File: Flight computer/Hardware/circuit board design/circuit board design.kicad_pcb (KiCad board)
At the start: 4 copper layers, 31.7 x 82.6 mm, 86 parts, among them J1 Conn_01x04, J2 USB_B_Micro, J3 Screw_Terminal_01x04, J4 Conn_01x02, J5 Screw_Terminal_01x04, J6 Conn_Coaxial, J7 Conn_Coaxial, U1 IIS2MDC, U10 BMI088, U11 ATSAML21J18B-AUT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

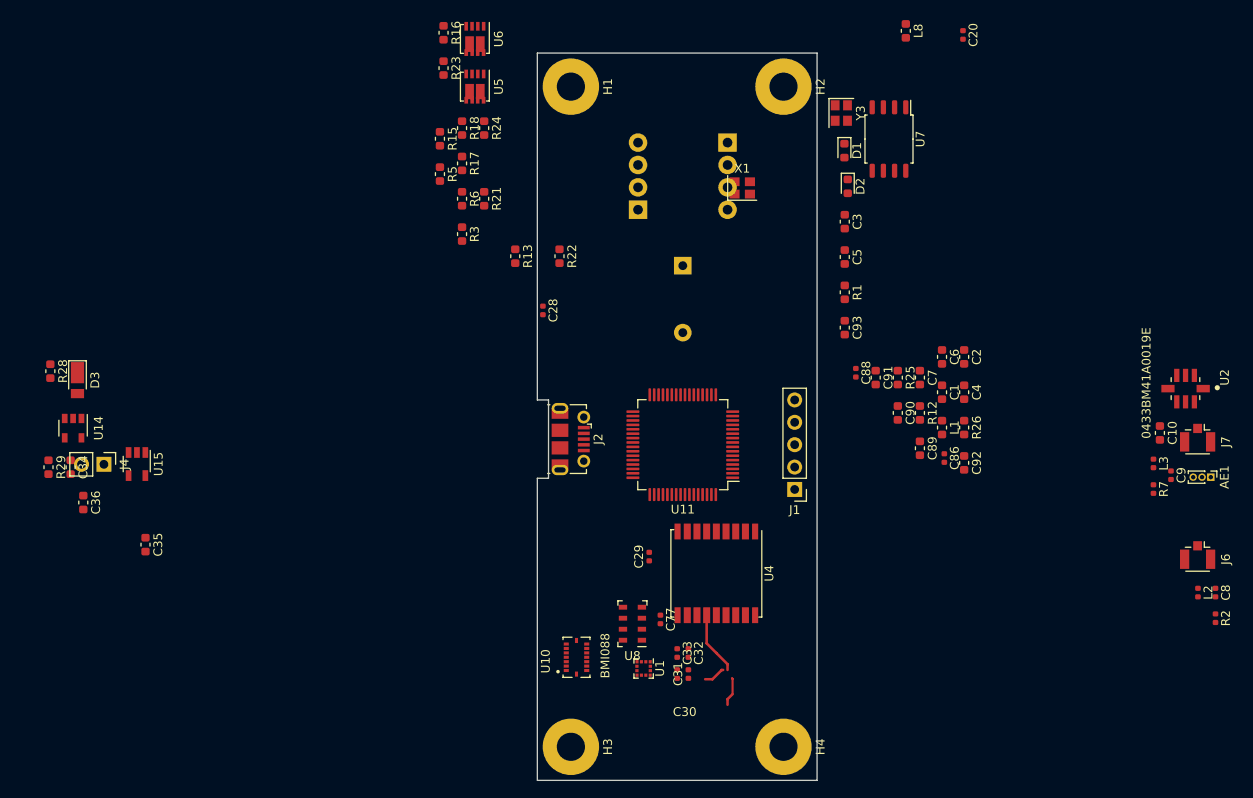
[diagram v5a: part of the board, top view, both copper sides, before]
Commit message: updated the datasheet links and sites to purchase
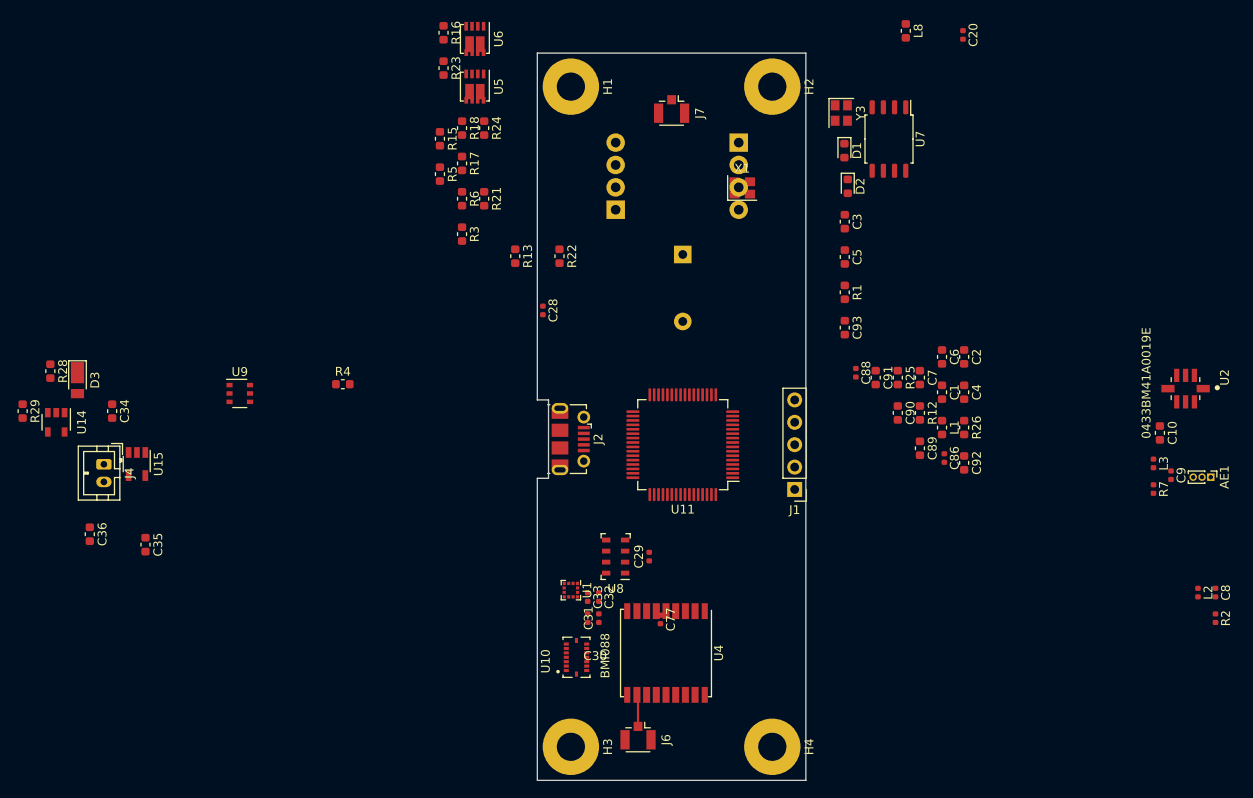
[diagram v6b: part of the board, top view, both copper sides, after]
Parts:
- added R4: 1K, Resistor_SMD:R_0603_1608Metric, F.Cu at (229.4, 284.0)
- added U9: STF202-22T1G, Package_SO:TSOP-6_1.65x3.05mm_P0.95mm, F.Cu at (217.7, 285.0)
- D1: value LED -> RED_LED
- D2: value LED -> BLUE_LED
- J1: value Conn_01x04 -> Conn_01x05
- J4: footprint Connector_PinHeader_2.54mm:PinHeader_1x02_P2.54mm_Vertical -> Connector_JST:JST_PH_B2B-PH-K_1x02_P2.00mm_Vertical
- moved J7 70.4 mm to (266.7, 252.7)
- moved J6 66.7 mm to (262.9, 323.9)
- moved U1 12.1 mm to (255.3, 307.3)
- moved C31 12.0 mm to (258.4, 310.5)
- moved C32 12.0 mm to (258.4, 308.1)
- moved C30 12.0 mm to (257.2, 310.5)
- moved C33 12.0 mm to (257.2, 308.1)
- moved U4 10.7 mm to (266.1, 314.5)
- moved C34 7.92 mm to (203.2, 287.0)
- moved U8 7.85 mm to (260.4, 303.5)
- moved R29 7.01 mm to (193.0, 287.0)
- moved C36 3.67 mm to (200.7, 301.0)
- moved J5 2.54 mm to (260.4, 264.2)
- moved U14 2.03 mm to (196.8, 288.3)
- moved BZ1 1.27 mm to (268.0, 269.2)
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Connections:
- net Net-(D3-Pad2) renamed VBUS
- J1 pad 5: (no net) -> Net-(C89-Pad1)
- J2 pad 2: /power_supply/USB_DM -> Net-(J2-Pad2)
- J2 pad 3: /MCU/USB_DM -> Net-(J2-Pad3)
- J3 pad 1: Vdrive -> Net-(J3-Pad1)
- J3 pad 3: Vdrive -> Net-(J3-Pad1)
- J5 pad 1: Vdrive -> Net-(J3-Pad1)
- J5 pad 3: Vdrive -> Net-(J3-Pad1)
- U11 pad 40: Net-(U11-Pad40) -> /MCU/ARMED
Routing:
- net Net-(U4-Pad13): track 6.56 -> 0.00 mm
- net Net-(J6-Pad1): track 0.00 -> 3.63 mm
- net Net-(ANT1-Pad1): track 3.29 -> 0.00 mm
- net Net-(U12-Pad6): track 2.48 -> 0.00 mm
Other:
- board size 31.7 x 82.6 mm -> 30.5 x 82.6 mm
